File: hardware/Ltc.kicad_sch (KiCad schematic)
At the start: 23 parts, among them CN1 4x100nF, CN3 4x100nF, CN5 4x100nF, CN7 4x100nF, IC1 LTC6804HG-1#PBF

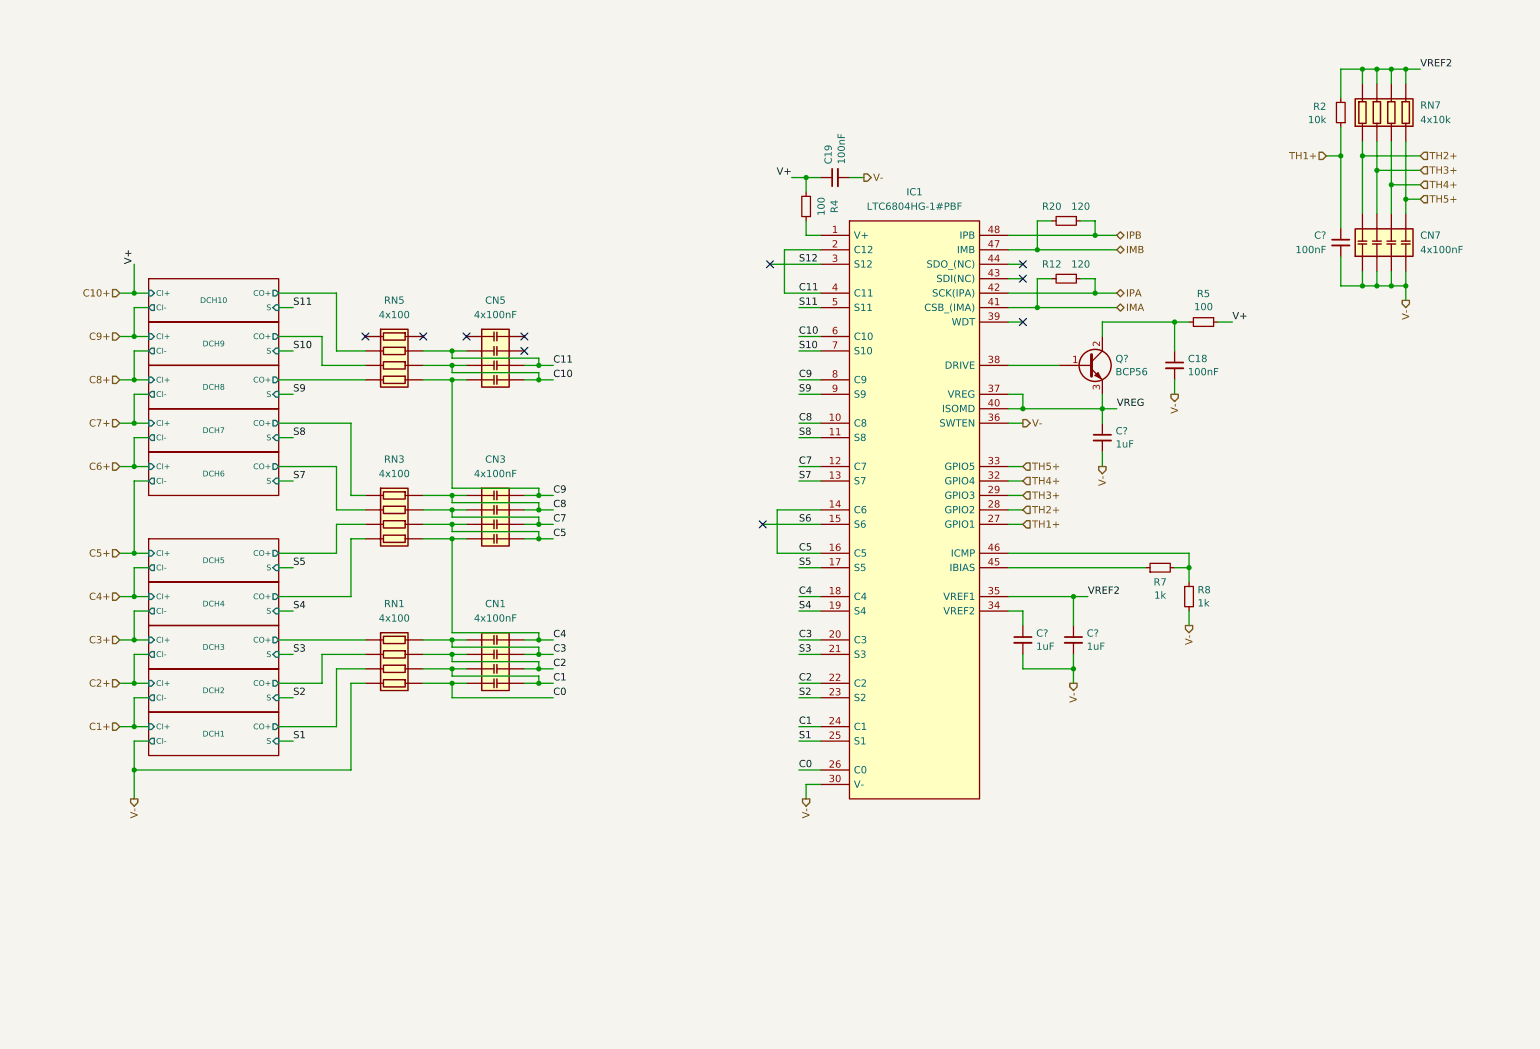
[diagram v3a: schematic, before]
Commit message: added temp disconnect, beautify schematic
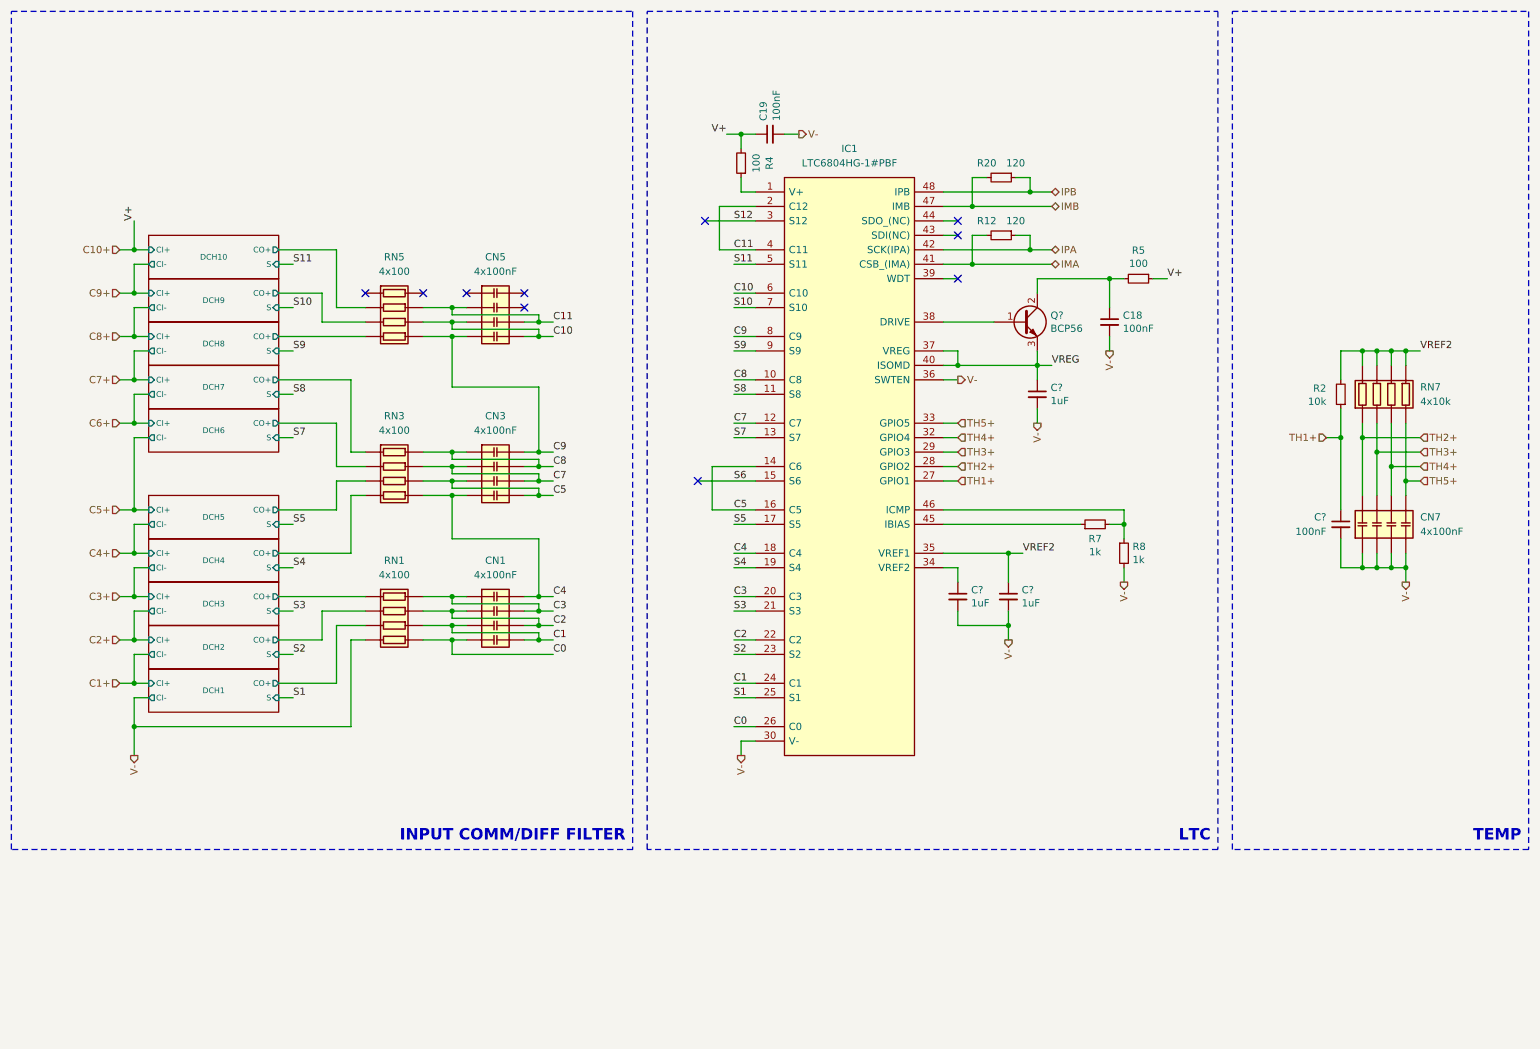
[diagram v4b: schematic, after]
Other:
- note added: "INPUT COMM/DIFF FILTER"
- note added: "LTC"
- note added: "TEMP"
- moved on the sheet: C18, C19, C?, CN1, CN3, CN5, CN7, IC1, Q?, R12, R2, R20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

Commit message: replaced signal transformer with rated capacitors, made the design more general for future use
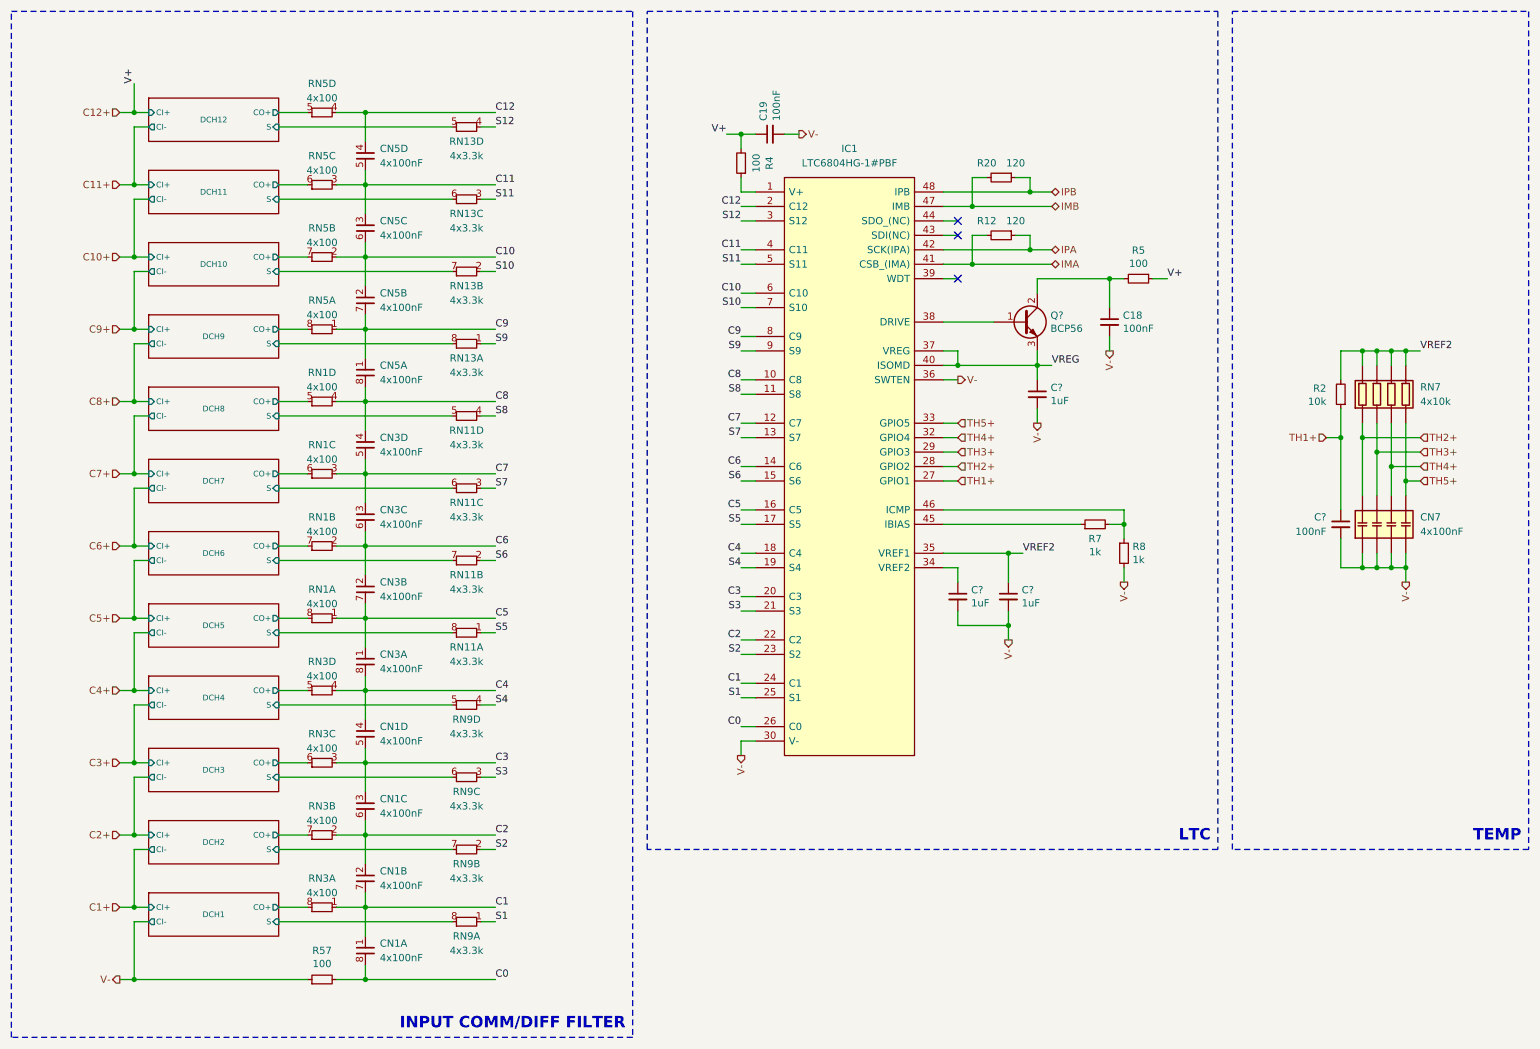
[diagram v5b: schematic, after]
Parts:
- removed RN1, RN3, RN5: 4x100, Samacsys:EXBV8V101JV, symbol exb-v8v101jv:EXB-V8V101JV
- added unit 3 of CN1
- added unit 4 of CN1
- added unit 2 of CN1
- added unit 3 of CN3
- added unit 2 of CN3
- added unit 4 of CN3
- added unit 3 of CN5
- added unit 4 of CN5
- added unit 2 of CN5
- added R57: 100, Resistor_SMD:R_0603_1608Metric, symbol PUTM_EV_BMS_HV_Slave_2021-rescue:R_Small-Device
- added RN1, RN3, RN5: 4x100, Resistor_SMD:R_Array_Convex_4x0603, symbol Device:R_Pack04_Split
- added RN11, RN13, RN9: 4x3.3k, Resistor_SMD:R_Array_Convex_4x0603, symbol Device:R_Pack04_Split
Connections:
- net C0: now also CN1.8 (R1.2), R57.2; no longer CN1.4 (R4.1)
- net C1: now also CN1.1 (R1.1), CN1.7 (R2.2), RN3.1 (R1.1); no longer CN1.3 (R3.1), CN1.5 (R4.2)
- net C10: now also CN5.2 (R2.1), CN5.6 (R4.1), RN5.2 (R2.1); no longer CN5.3 (R3.1), CN5.5 (R4.2)
- net C10+: no longer C19.1, R4.2, R5.1
- net C11: now also CN5.3 (R3.1), CN5.5 (R4.2), RN5.3 (R3.1); no longer CN5.2 (R2.1), CN5.6 (R3.2), IC1.2 (C12)
- net C2: now also CN1.2 (R2.1), CN1.6 (R4.1), RN3.2 (R2.1); no longer CN1.2 (R2.1), CN1.6 (R3.2)
- net C3: now also CN1.3 (R3.1), CN1.5 (R4.2), RN3.3 (R3.1); no longer CN1.1 (R1.1), CN1.7 (R2.2)
- net C4: now also CN3.8 (R1.2), CN1.4 (R4.1), RN3.4 (R4.1); no longer CN1.8 (R1.2), CN3.4 (R4.1)
- net C5: now also CN3.1 (R1.1), CN3.7 (R2.2), RN1.1 (R1.1); no longer CN3.3 (R3.1), CN3.5 (R4.2), IC1.14 (C6)
- net C7: now also CN3.3 (R3.1), CN3.5 (R4.2), RN1.3 (R3.1); no longer CN3.2 (R2.1), CN3.6 (R3.2)
- net C8: now also CN5.8 (R1.2), CN3.4 (R4.1), RN1.4 (R4.1); no longer CN3.1 (R1.1), CN3.7 (R2.2)
- net C9: now also CN5.1 (R1.1), CN5.7 (R2.2), RN5.1 (R1.1); no longer CN3.8 (R1.2), CN5.4 (R4.1)
- net DCH1/CO+: now also RN3.8 (R1.2)
- net DCH10/CO+: now also RN5.7 (R2.2)
- net DCH2/CO+: now also RN3.7 (R2.2)
- net DCH3/CO+: now also RN3.6 (R3.2)
- net DCH4/CO+: now also RN3.5 (R4.2)
- net DCH5/CO+: now also RN1.8 (R1.2)
- net DCH6/CO+: now also RN1.7 (R2.2)
- net DCH7/CO+: now also RN1.6 (R3.2)
- net DCH8/CO+: now also RN1.5 (R4.2)
- net DCH9/CO+: now also RN5.8 (R1.2)
- net S1: now also RN9.1 (R1.1)
- net S10: now also RN13.2 (R2.1)
- net S11: now also RN13.3 (R3.1)
- net S12: now also RN13.4 (R4.1)
- net S2: now also RN9.2 (R2.1)
- net S3: now also RN9.3 (R3.1)
- net S4: now also RN9.4 (R4.1)
- net S5: now also RN11.1 (R1.1)
- net S6: now also RN11.2 (R2.1)
- net S7: now also RN11.3 (R3.1)
- net S8: now also RN11.4 (R4.1)
- net S9: now also RN13.1 (R1.1)
- net V-: now also R57.1
- new net C12: CN5.4 (R4.1), IC1.2 (C12), RN5.4 (R4.1)
- new net C12+: C19.1, R4.2, R5.1
- new net C6: CN3.2 (R2.1), CN3.6 (R4.1), IC1.14 (C6), RN1.2 (R2.1)
- new net DCH1/S: RN9.8 (R1.2)
- new net DCH10/S: RN13.7 (R2.2)
- new net DCH11/CO+: RN5.6 (R3.2)
- new net DCH11/S: RN13.6 (R3.2)
- new net DCH12/CO+: RN5.5 (R4.2)
- new net DCH12/S: RN13.5 (R4.2)
- new net DCH2/S: RN9.7 (R2.2)
- new net DCH3/S: RN9.6 (R3.2)
- new net DCH4/S: RN9.5 (R4.2)
- new net DCH5/S: RN11.8 (R1.2)
- new net DCH6/S: RN11.7 (R2.2)
- new net DCH7/S: RN11.6 (R3.2)
- new net DCH8/S: RN11.5 (R4.2)
- new net DCH9/S: RN13.8 (R1.2)
- no-connect marks 10 -> 3
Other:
- added sheet DCH11 (Discharge.kicad_sch)
- added sheet DCH12 (Discharge.kicad_sch)

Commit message: new schematic
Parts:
- removed RN11, RN13, RN9: 4x3.3k, Resistor_SMD:R_Array_Convex_4x0603, symbol Device:R_Pack04_Split
- added JP1, JP2: MES, Jumper:SolderJumper-2_P1.3mm_Bridged2Bar_RoundedPad1.0x1.5mm, symbol Jumper:SolderJumper_2_Bridged
- added SW1: SW_DIP_x02, Button_Switch_SMD:SW_DIP_SPSTx02_Slide_6.7x6.64mm_W6.73mm_P2.54mm_LowProfile_JPin, symbol Switch:SW_DIP_x02
- C?: now not fitted
- CN1, CN3, CN5, CN7: footprint Samacsys:CA064X104K4RACAUTO -> Resistor_SMD:R_Array_Convex_4x0603; now not fitted
- RN7: footprint Samacsys:EXBV8V101JV -> Resistor_SMD:R_Array_Convex_4x0603
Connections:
- net C1: now also JP1.1 (A), SW1.2
- net C12: no longer IC1.2 (C12)
- net TH1+: now also JP2.1 (A), SW1.1; no longer IC1.27 (GPIO1)
- new net SW_C1: JP1.2 (B), SW1.3
- new net SW_TH1+: IC1.27 (GPIO1), JP2.2 (B), SW1.4
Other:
- sheet DCH1 ports: added none; removed CI-
- sheet DCH10 ports: added none; removed CI-
- sheet DCH11 ports: added none; removed CI-
- sheet DCH12 ports: added none; removed CI-
- sheet DCH2 ports: added none; removed CI-
- sheet DCH3 ports: added none; removed CI-
- sheet DCH4 ports: added none; removed CI-
- sheet DCH5 ports: added none; removed CI-
- sheet DCH6 ports: added none; removed CI-
- sheet DCH7 ports: added none; removed CI-
- sheet DCH8 ports: added none; removed CI-
- sheet DCH9 ports: added none; removed CI-
- note added: "CELL/TEMP DISCONN"
- note added: "sprawdzic jeszcze tego sipa"
- moved on the sheet: R2, RN7

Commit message: layout done
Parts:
- removed CN1, CN3, CN5: 4x100nF, Resistor_SMD:R_Array_Convex_4x0603, symbol ca064x104k4racauto:CA064X104K4RACAUTO
- removed JP1, JP2: MES, Jumper:SolderJumper-2_P1.3mm_Bridged2Bar_RoundedPad1.0x1.5mm, symbol Jumper:SolderJumper_2_Bridged
- removed R57: 100, Resistor_SMD:R_0603_1608Metric, symbol PUTM_EV_BMS_HV_Slave_2021-rescue:R_Small-Device
- removed RN1, RN3, RN5: 4x100, Resistor_SMD:R_Array_Convex_4x0603, symbol Device:R_Pack04_Split
- removed SW1: SW_DIP_x02, Button_Switch_SMD:SW_DIP_SPSTx02_Slide_6.7x6.64mm_W6.73mm_P2.54mm_LowProfile_JPin, symbol Switch:SW_DIP_x02
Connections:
- net C0 is gone; now on net V-: IC1.26 (C0)
- net C1 is gone; now on net C1+: IC1.24 (C1)
- net C10 is gone; now on net C10+: IC1.6 (C10)
- net C11 is gone; now on net C11+: IC1.4 (C11)
- net C2 is gone; now on net C2+: IC1.22 (C2)
- net C3 is gone; now on net C3+: IC1.20 (C3)
- net C4 is gone; now on net C4+: IC1.18 (C4)
- net C5 is gone; now on net C5+: IC1.16 (C5)
- net C6 is gone; now on net C6+: IC1.14 (C6)
- net C7 is gone; now on net C7+: IC1.12 (C7)
- net C8 is gone; now on net C8+: IC1.10 (C8)
- net C9 is gone; now on net C9+: IC1.8 (C9)
- net SW_TH1+ is gone; now on net TH1+: IC1.27 (GPIO1)
- net C12+: now also IC1.2 (C12)
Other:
- sheet DCH1 ports: added C; removed CI+, CO+
- sheet DCH10 ports: added C; removed CI+, CO+
- sheet DCH11 ports: added C; removed CI+, CO+
- sheet DCH12 ports: added C; removed CI+, CO+
- sheet DCH2 ports: added C; removed CI+, CO+
- sheet DCH3 ports: added C; removed CI+, CO+
- sheet DCH4 ports: added C; removed CI+, CO+
- sheet DCH5 ports: added C; removed CI+, CO+
- sheet DCH6 ports: added C; removed CI+, CO+
- sheet DCH7 ports: added C; removed CI+, CO+
- sheet DCH8 ports: added C; removed CI+, CO+
- sheet DCH9 ports: added C; removed CI+, CO+

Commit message: new balancing schematic
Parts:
- removed R12, R20: 120, Resistor_SMD:R_0603_1608Metric, symbol PUTM_EV_BMS_HV_Slave_2021-rescue:R_Small-Device
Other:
- removed sheet DCH10
- removed sheet DCH11
- removed sheet DCH12
- removed sheet DCH2
- removed sheet DCH3
- removed sheet DCH4
- removed sheet DCH5
- removed sheet DCH6
- removed sheet DCH7
- removed sheet DCH8
- removed sheet DCH9
- sheet DCH1 ports: added none; removed C, S
